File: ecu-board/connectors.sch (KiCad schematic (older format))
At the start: 31 parts, among them J10 Injector connector, J13 Chrankshaft Hall connector, J14 Camshaft Hall connector, J2 Battery power conenctor, J4 Motor connector, J5 Serial DB9 connector, J8 IAT connector, J9 CLT connector

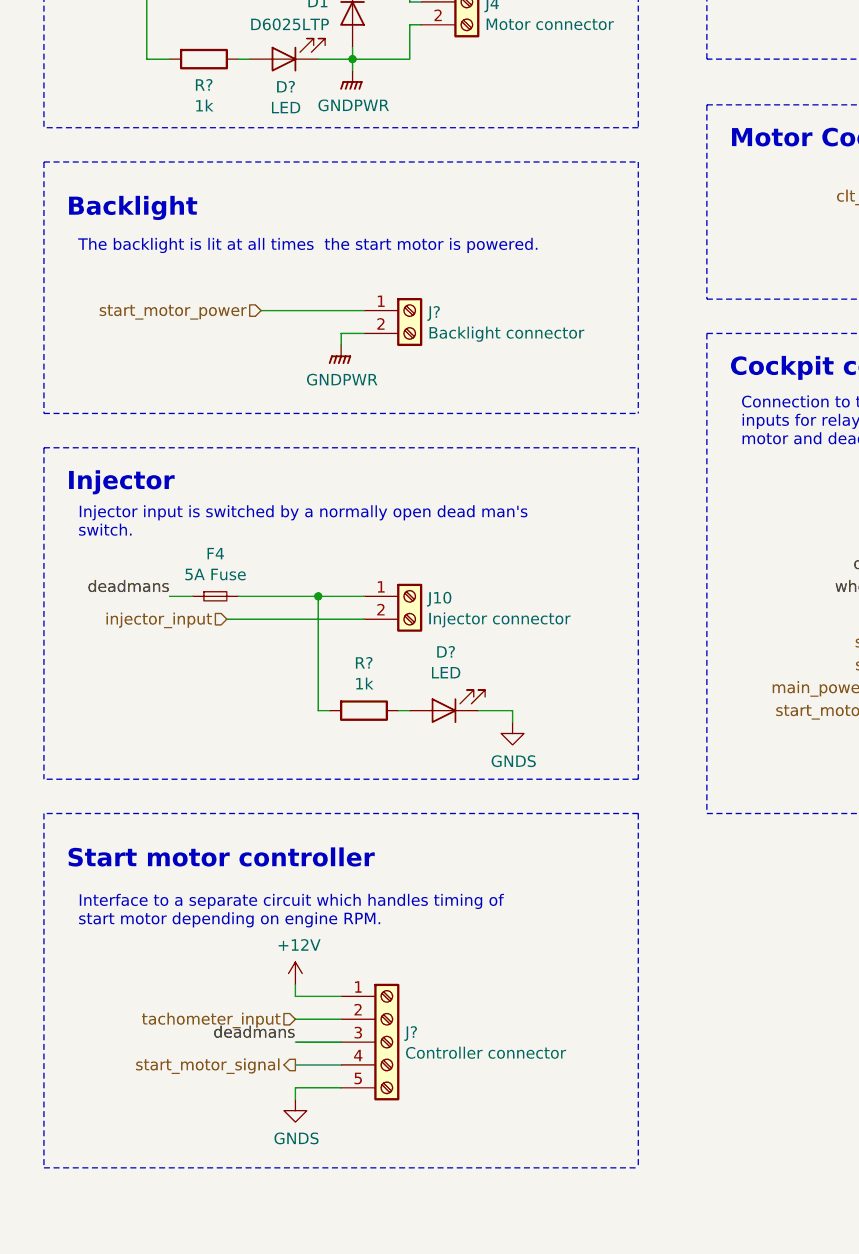
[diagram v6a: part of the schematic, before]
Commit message: Add backlight fuse. Closes #31.
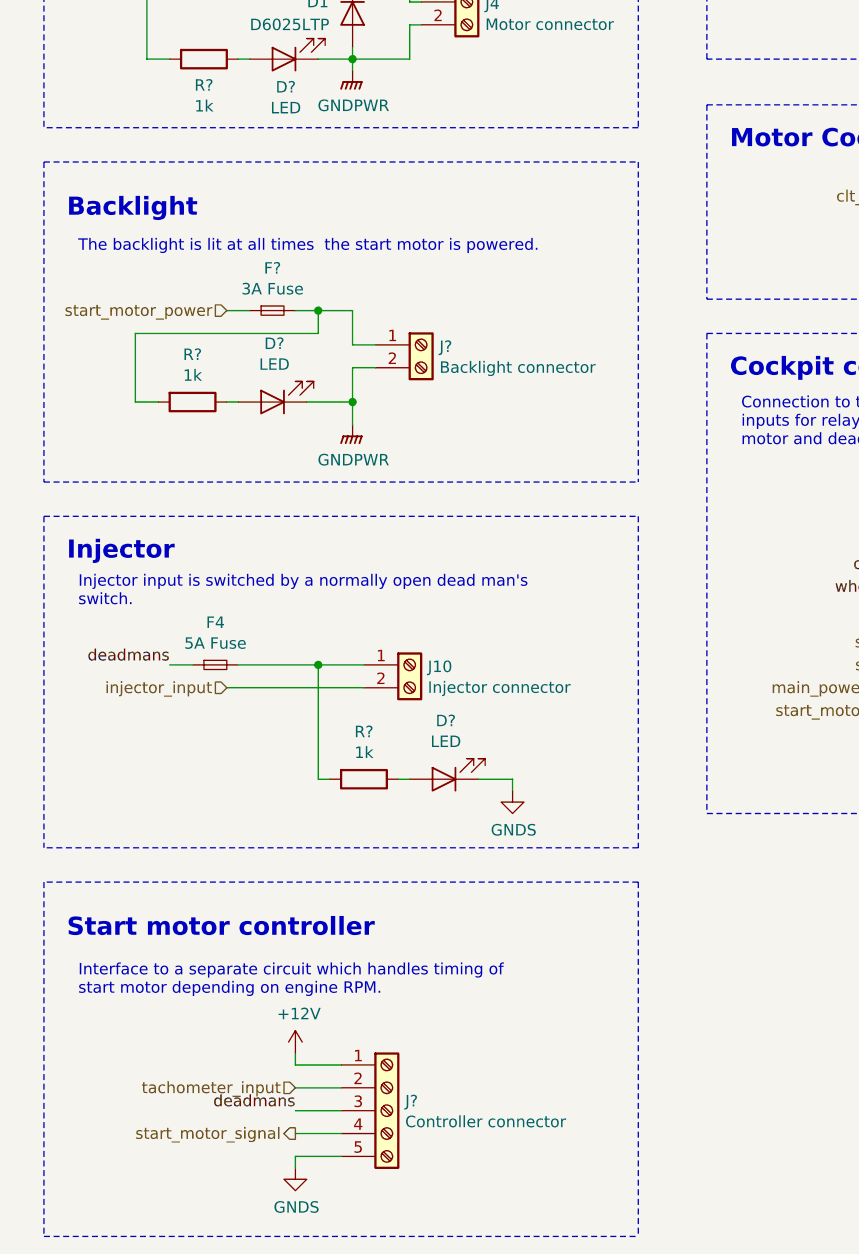
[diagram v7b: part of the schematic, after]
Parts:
- added D?: LED, LEDs:LED_D3.0mm, symbol Device:LED
- added F?: 3A Fuse, symbol Device:Fuse_Small
- added R?: 1k, symbol Device:R
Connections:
- net GNDPWR: now also D?.1 (K)
- net start_motor_power: now also F?.1; no longer J?.1 (Pin_1)
- new net: F?.2, J?.1 (Pin_1), R?.2
- new net: D?.2 (A), R?.1
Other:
- moved on the sheet: D?, F4, J10, J?, R?

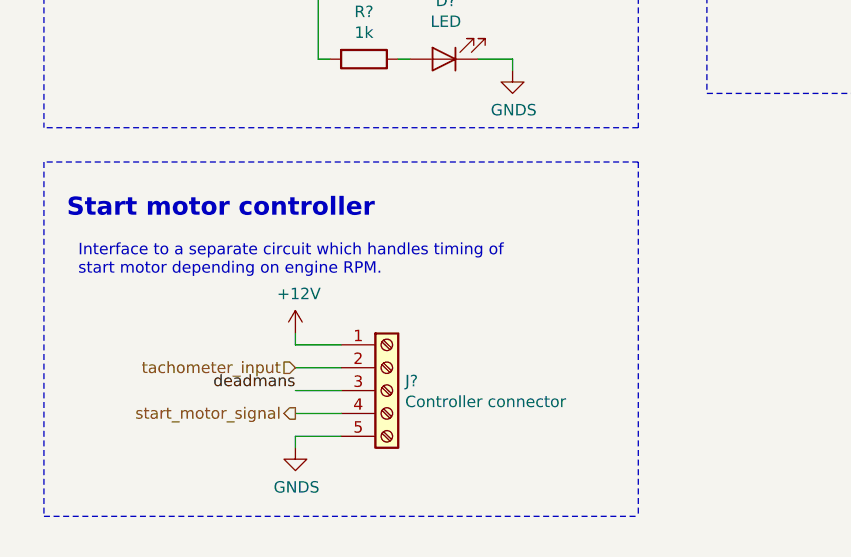
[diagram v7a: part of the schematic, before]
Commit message: Add info about start motor.
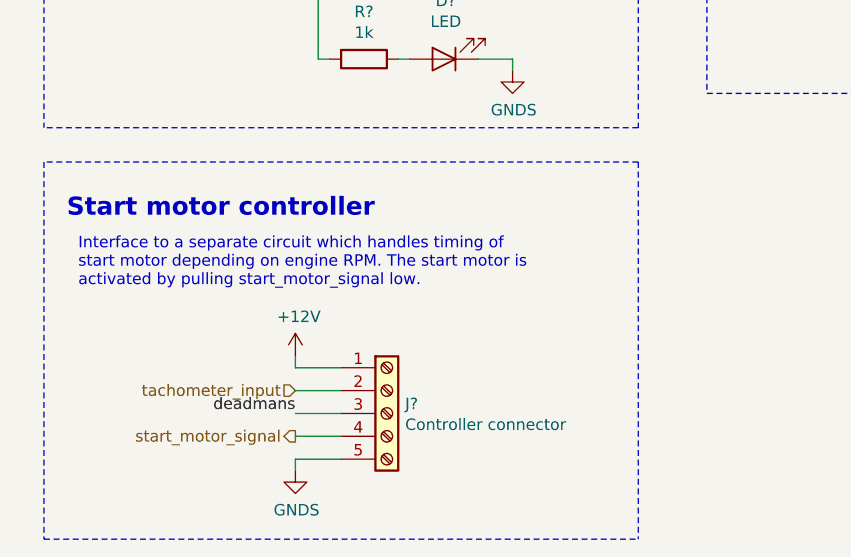
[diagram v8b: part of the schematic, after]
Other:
- note added: "Interface to a separate circuit which handles timing of \nstart motor depending on engine RPM. The start motor is \nactivated by pulling start_motor_signal low."
- note removed: "Interface to a separate circuit which handles timing of \nstart motor depending on engine RPM."
- moved on the sheet: J?
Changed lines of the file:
@@
 	1    0    0    -1
 $EndComp
-Text HLabel 1900 8200 0    50   Input ~ 0
+Text HLabel 1900 8300 0    50   Input ~ 0
 tachometer_input
 Wire Wire Line
@@
 	11000 900  11000 5200
 Wire Notes Line
-	800  8850 3400 8850
+	800  8950 3400 8950
 Wire Notes Line
 	3400 7300 800  7300
@@
 L power:+12V #PWR?
 U 1 1 5CA43097
-P 1900 8050
-F 0 "#PWR?" H 1900 7900 50  0001 C CNN
-F 1 "+12V" H 1915 8223 50  0000 C CNN
-F 2 "" H 1900 8050 50  0001 C CNN
-F 3 "" H 1900 8050 50  0001 C CNN
-	1    1900 8050
+P 1900 8150
+F 0 "#PWR?" H 1900 8000 50  0001 C CNN
+F 1 "+12V" H 1915 8323 50  0000 C CNN
+F 2 "" H 1900 8150 50  0001 C CNN
+F 3 "" H 1900 8150 50  0001 C CNN
+	1    1900 8150
 	1    0    0    -1
 $EndComp
@@
 L power:GNDS #PWR?
 U 1 1 5CA430CE
-P 1900 8550
-F 0 "#PWR?" H 1900 8300 50  0001 C CNN
-F 1 "GNDS" H 1905 8377 50  0000 C CNN
-F 2 "" H 1900 8550 50  0001 C CNN
-F 3 "" H 1900 8550 50  0001 C CNN
-	1    1900 8550
+P 1900 8650
+F 0 "#PWR?" H 1900 8400 50  0001 C CNN
+F 1 "GNDS" H 1905 8477 50  0000 C CNN
+F 2 "" H 1900 8650 50  0001 C CNN
+F 3 "" H 1900 8650 50  0001 C CNN
+	1    1900 8650
 	1    0    0    -1
 $EndComp
@@
 L Connector:Screw_Terminal_01x05 J?
 U 1 1 5CA4D167
-P 2300 8300
-F 0 "J?" H 2380 8342 50  0000 L CNN
-F 1 "Controller connector" H 2380 8251 50  0000 L CNN
-F 2 "" H 2300 8300 50  0001 C CNN
-F 3 "~" H 2300 8300 50  0001 C CNN
-	1    2300 8300
-	1    0    0    -1
-$EndComp
-Wire Wire Line
-	1900 8550 1900 8500
-Wire Wire Line
-	1900 8500 2100 8500
-Wire Wire Line
-	2100 8400 1900 8400
-Wire Wire Line
-	1900 8300 2100 8300
-Wire Wire Line
-	2100 8200 1900 8200
-Wire Wire Line
-	1900 8050 1900 8100
-Wire Wire Line
-	1900 8100 2100 8100
-Text Notes 950  7800 0    50   ~ 0
-Interface to a separate circuit which handles timing of \nstart motor depending on engine RPM.
-Text Label 1900 8300 2    50   ~ 0
+P 2300 8400
+F 0 "J?" H 2380 8442 50  0000 L CNN
+F 1 "Controller connector" H 2380 8351 50  0000 L CNN
+F 2 "" H 2300 8400 50  0001 C CNN
+F 3 "~" H 2300 8400 50  0001 C CNN
+	1    2300 8400
+	1    0    0    -1
+$EndComp
+Wire Wire Line
+	1900 8650 1900 8600
+Wire Wire Line
+	1900 8600 2100 8600
+Wire Wire Line
+	2100 8500 1900 8500
+Wire Wire Line
+	1900 8400 2100 8400
+Wire Wire Line
+	2100 8300 1900 8300
+Wire Wire Line
+	1900 8150 1900 8200
+Wire Wire Line
+	1900 8200 2100 8200
+Text Notes 950  7850 0    50   ~ 0
+Interface to a separate circuit which handles timing of \nstart motor depending on engine RPM. The start motor is \nactivated by pulling start_motor_signal low.
+Text Label 1900 8400 2    50   ~ 0
 deadmans
 Text Label 1350 6350 2    50   ~ 0
 deadmans
-Text HLabel 1900 8400 0    50   Output ~ 0
+Text HLabel 1900 8500 0    50   Output ~ 0
 start_motor_signal
-Wire Notes Line
-	3400 7300 3400 8850
-Wire Notes Line
-	800  7300 800  8850
 $Comp
 L Device:LED D?
@@
 Wire Notes Line
 	800  4150 800  5550
+Wire Notes Line
+	3400 7300 3400 8950
+Wire Notes Line
+	800  7300 800  8950
 $EndSCHEMATC
